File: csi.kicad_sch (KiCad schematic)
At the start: 90 parts, among them J701 WE_68715014522, J702 WE_68715014522, Q701 BSS138W-7-F, Q702 BSS138W-7-F, Q703 BSS138W-7-F, Q704 BSS138W-7-F, U701 PCA9547BS, U702 AP22615, U703 AP22615, U704 NX3DV642, U705 NX3DV642, U706 AP22615, U707 AP22615

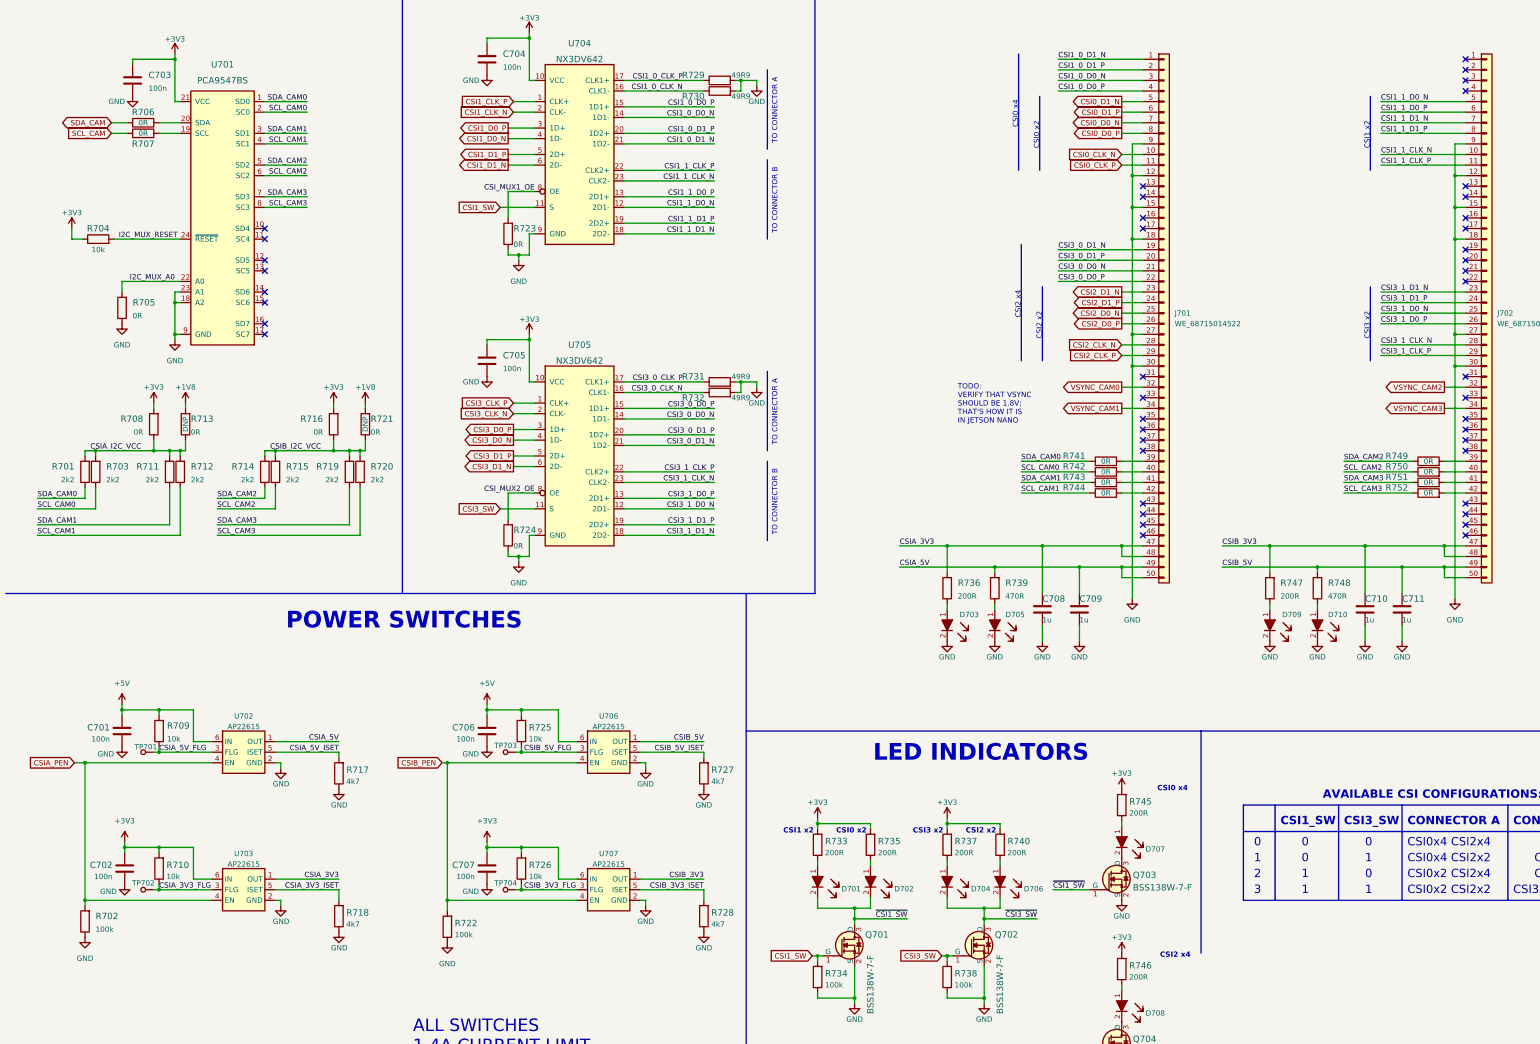
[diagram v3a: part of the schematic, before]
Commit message: Unified schematic look of ethernet sheet, improved shielding of eth connector, replaced gnd symbols
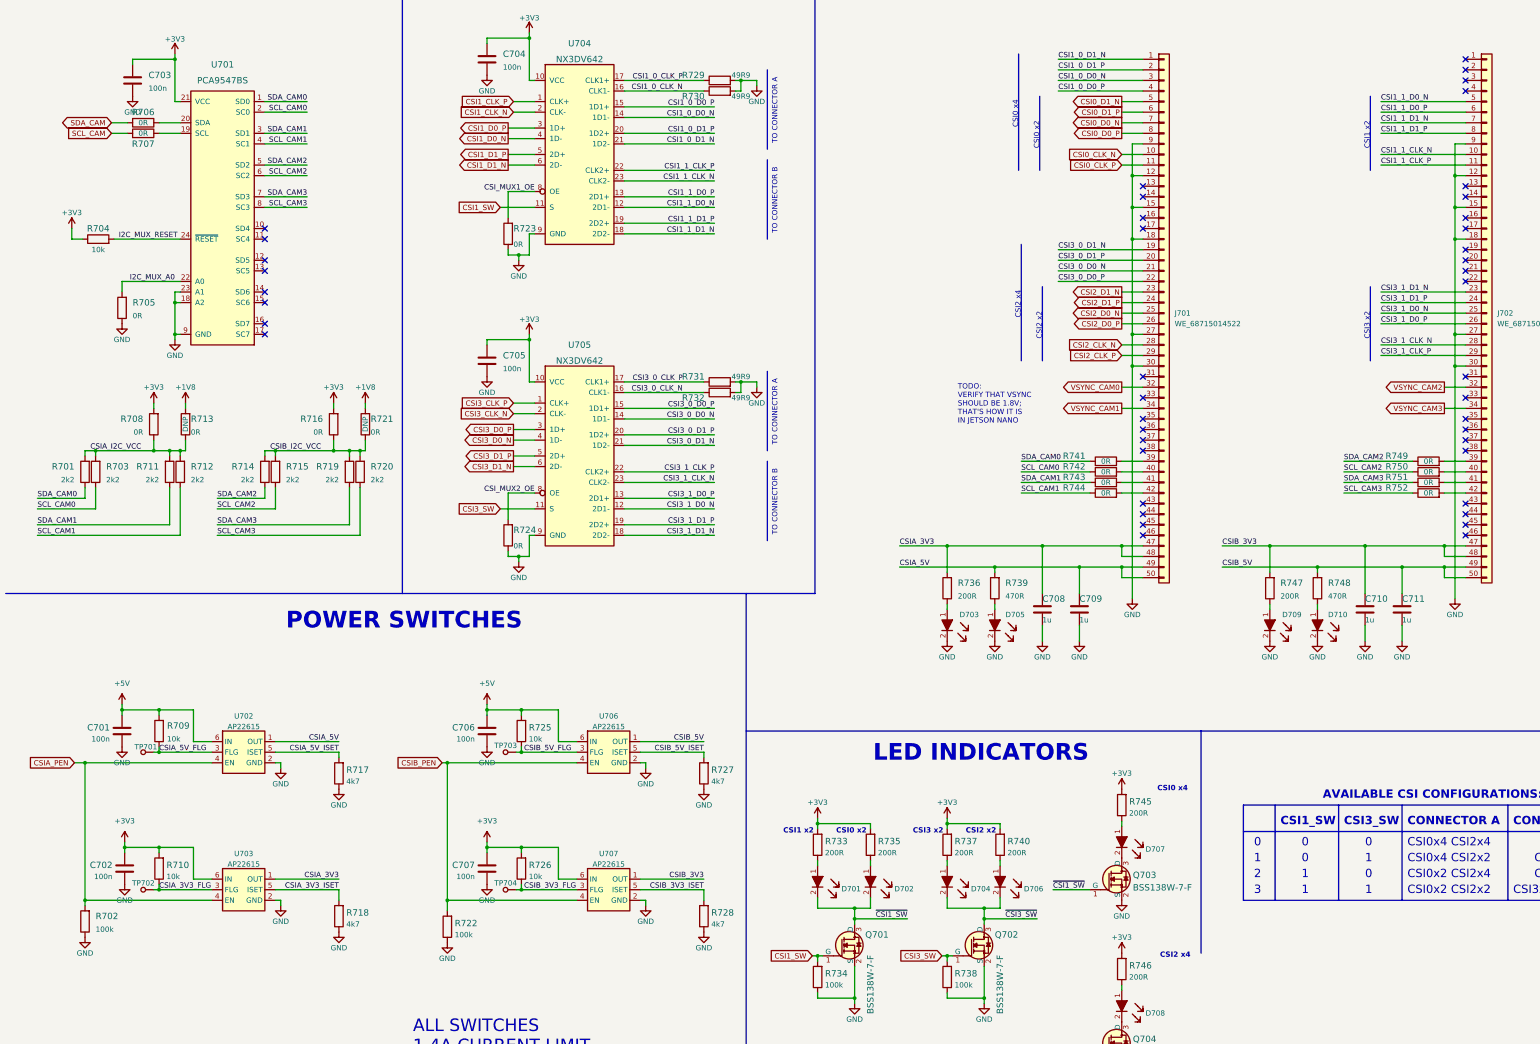
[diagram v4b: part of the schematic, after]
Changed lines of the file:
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@@
       (effects (font (size 1.27 1.27)) hide)
     )
-    (property "Value" "GND" (id 1) (at 135.89 91.44 0))
+    (property "Value" "GND" (id 1) (at 135.89 90.17 0))
     (property "Footprint" "" (id 2) (at 135.89 86.36 0)
       (effects (font (size 1.27 1.27)) hide)
@@
       (effects (font (size 1.27 1.27)) hide)
     )
-    (property "Value" "GND" (id 1) (at 283.21 172.72 0))
+    (property "Value" "GND" (id 1) (at 283.21 171.45 0))
     (property "Footprint" "" (id 2) (at 283.21 167.64 0)
       (effects (font (size 1.27 1.27)) hide)
@@
       (effects (font (size 1.27 1.27)) hide)
     )
-    (property "Value" "GND" (id 1) (at 118.745 255.27 0))
+    (property "Value" "GND" (id 1) (at 118.745 254 0))
     (property "Footprint" "" (id 2) (at 118.745 250.19 0)
       (effects (font (size 1.27 1.27)) hide)
@@
       (effects (font (size 1.27 1.27)) hide)
     )
-    (property "Value" "GND" (id 1) (at 31.75 254 0))
+    (property "Value" "GND" (id 1) (at 31.75 252.73 0))
     (property "Footprint" "" (id 2) (at 31.75 248.92 0)
       (effects (font (size 1.27 1.27)) hide)
@@
       (effects (font (size 1.27 1.27)) hide)
     )
-    (property "Value" "GND" (id 1) (at 90.805 251.46 0)
-      (effects (font (size 1.27 1.27)) (justify left))
-    )
+    (property "Value" "GND" (id 1) (at 92.71 251.46 0))
     (property "Footprint" "" (id 2) (at 92.71 247.65 0)
       (effects (font (size 1.27 1.27)) hide)
@@
       (effects (font (size 1.27 1.27)) hide)
     )
-    (property "Value" "GND" (id 1) (at 126.3651 237.9238 0)
-      (effects (font (size 1.27 1.27)) (justify left))
-    )
+    (property "Value" "GND" (id 1) (at 128.27 240.03 0))
     (property "Footprint" "" (id 2) (at 128.27 236.22 0)
       (effects (font (size 1.27 1.27)) hide)
@@
       (effects (font (size 1.27 1.27)) hide)
     )
-    (property "Value" "GND" (id 1) (at 126.3651 204.9038 0)
-      (effects (font (size 1.27 1.27)) (justify left))
-    )
+    (property "Value" "GND" (id 1) (at 128.27 207.01 0))
     (property "Footprint" "" (id 2) (at 128.27 203.2 0)
       (effects (font (size 1.27 1.27)) hide)
@@
       (effects (font (size 1.27 1.27)) hide)
     )
-    (property "Value" "GND" (id 1) (at 90.805 217.17 0)
-      (effects (font (size 1.27 1.27)) (justify left))
-    )
+    (property "Value" "GND" (id 1) (at 92.71 217.17 0))
     (property "Footprint" "" (id 2) (at 92.71 213.36 0)
       (effects (font (size 1.27 1.27)) hide)
@@
       (effects (font (size 1.27 1.27)) hide)
     )
-    (property "Value" "GND" (id 1) (at 76.835 245.11 0)
-      (effects (font (size 1.27 1.27)) (justify left))
-    )
+    (property "Value" "GND" (id 1) (at 78.74 245.11 0))
     (property "Footprint" "" (id 2) (at 78.74 241.3 0)
       (effects (font (size 1.27 1.27)) hide)
@@
       (effects (font (size 1.27 1.27)) hide)
     )
-    (property "Value" "GND" (id 1) (at 76.835 212.09 0)
-      (effects (font (size 1.27 1.27)) (justify left))
-    )
+    (property "Value" "GND" (id 1) (at 78.74 212.09 0))
     (property "Footprint" "" (id 2) (at 78.74 208.28 0)
       (effects (font (size 1.27 1.27)) hide)
@@
       (effects (font (size 1.27 1.27)) hide)
     )
-    (property "Value" "GND" (id 1) (at 39.3701 237.9238 0)
-      (effects (font (size 1.27 1.27)) (justify left))
-    )
+    (property "Value" "GND" (id 1) (at 41.275 240.03 0))
     (property "Footprint" "" (id 2) (at 41.275 236.22 0)
       (effects (font (size 1.27 1.27)) hide)
@@
       (effects (font (size 1.27 1.27)) hide)
     )
-    (property "Value" "GND" (id 1) (at 360.68 172.72 0))
+    (property "Value" "GND" (id 1) (at 360.68 171.45 0))
     (property "Footprint" "" (id 2) (at 360.68 167.64 0)
       (effects (font (size 1.27 1.27)) hide)
@@
       (effects (font (size 1.27 1.27)) hide)
     )
-    (property "Value" "GND" (id 1) (at 124.46 43.18 0))
+    (property "Value" "GND" (id 1) (at 128.27 45.72 0))
     (property "Footprint" "" (id 2) (at 128.27 41.91 0)
       (effects (font (size 1.27 1.27)) hide)
@@
       (effects (font (size 1.27 1.27)) hide)
     )
-    (property "Value" "GND" (id 1) (at 135.89 163.83 0))
+    (property "Value" "GND" (id 1) (at 135.89 162.56 0))
     (property "Footprint" "" (id 2) (at 135.89 158.75 0)
       (effects (font (size 1.27 1.27)) hide)
@@
       (effects (font (size 1.27 1.27)) hide)
     )
-    (property "Value" "GND" (id 1) (at 39.37 48.26 0))
+    (property "Value" "GND" (id 1) (at 43.18 50.8 0))
     (property "Footprint" "" (id 2) (at 43.18 46.99 0)
       (effects (font (size 1.27 1.27)) hide)
@@
       (effects (font (size 1.27 1.27)) hide)
     )
-    (property "Value" "GND" (id 1) (at 40.64 106.68 0))
+    (property "Value" "GND" (id 1) (at 40.64 105.41 0))
     (property "Footprint" "" (id 2) (at 40.64 101.6 0)
       (effects (font (size 1.27 1.27)) hide)
@@
       (effects (font (size 1.27 1.27)) hide)
     )
-    (property "Value" "GND" (id 1) (at 124.46 115.57 0))
+    (property "Value" "GND" (id 1) (at 128.27 118.11 0))
     (property "Footprint" "" (id 2) (at 128.27 114.3 0)
       (effects (font (size 1.27 1.27)) hide)
@@
       (effects (font (size 1.27 1.27)) hide)
     )
-    (property "Value" "GND" (id 1) (at 38.7351 204.9038 0)
-      (effects (font (size 1.27 1.27)) (justify left))
-    )
+    (property "Value" "GND" (id 1) (at 40.64 207.01 0))
     (property "Footprint" "" (id 2) (at 40.64 203.2 0)
       (effects (font (size 1.27 1.27)) hide)
@@
       (effects (font (size 1.27 1.27)) hide)
     )
-    (property "Value" "GND" (id 1) (at 53.34 110.49 0))
+    (property "Value" "GND" (id 1) (at 53.34 109.22 0))
     (property "Footprint" "" (id 2) (at 53.34 105.41 0)
       (effects (font (size 1.27 1.27)) hide)

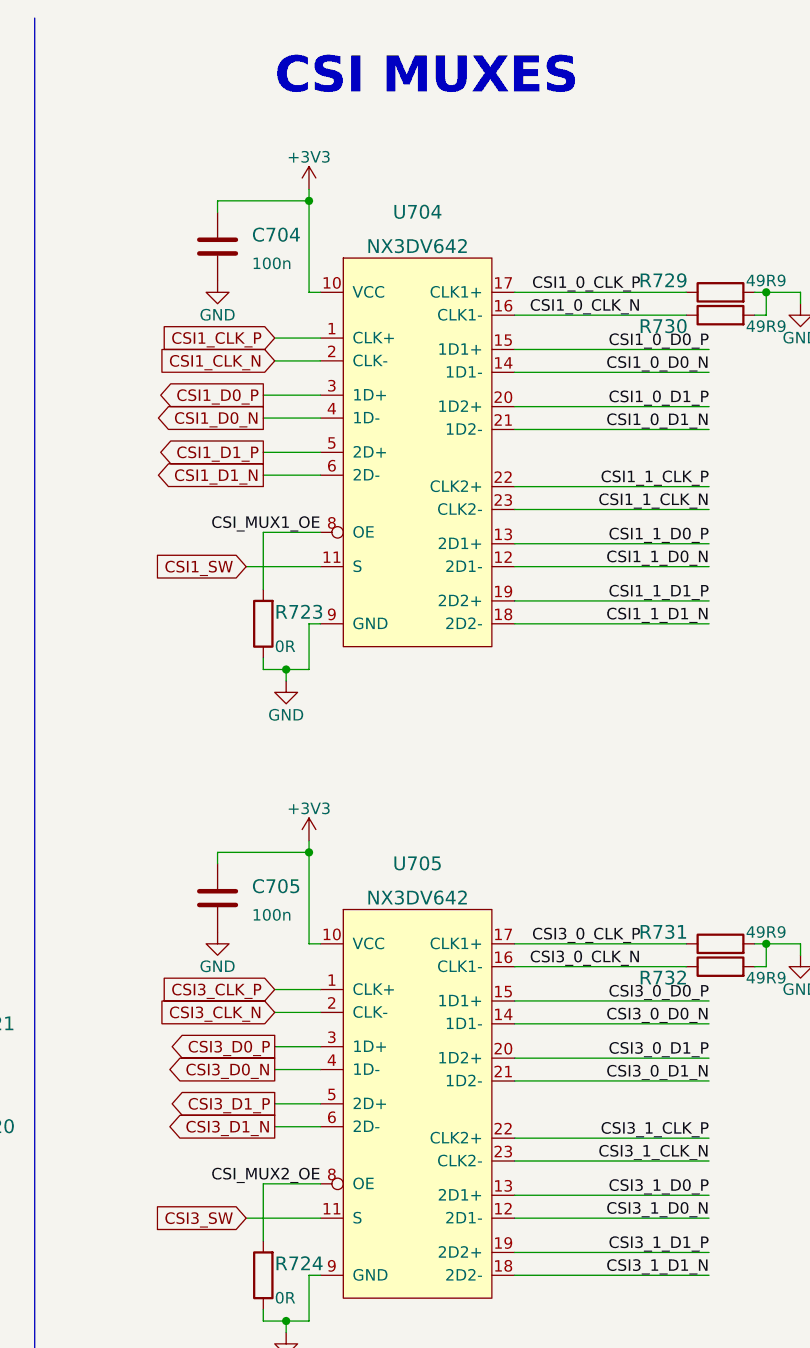
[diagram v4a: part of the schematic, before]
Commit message: Add CSI MUX labels and numbers to refer to on Block Diagram, update all GND symbols from global library
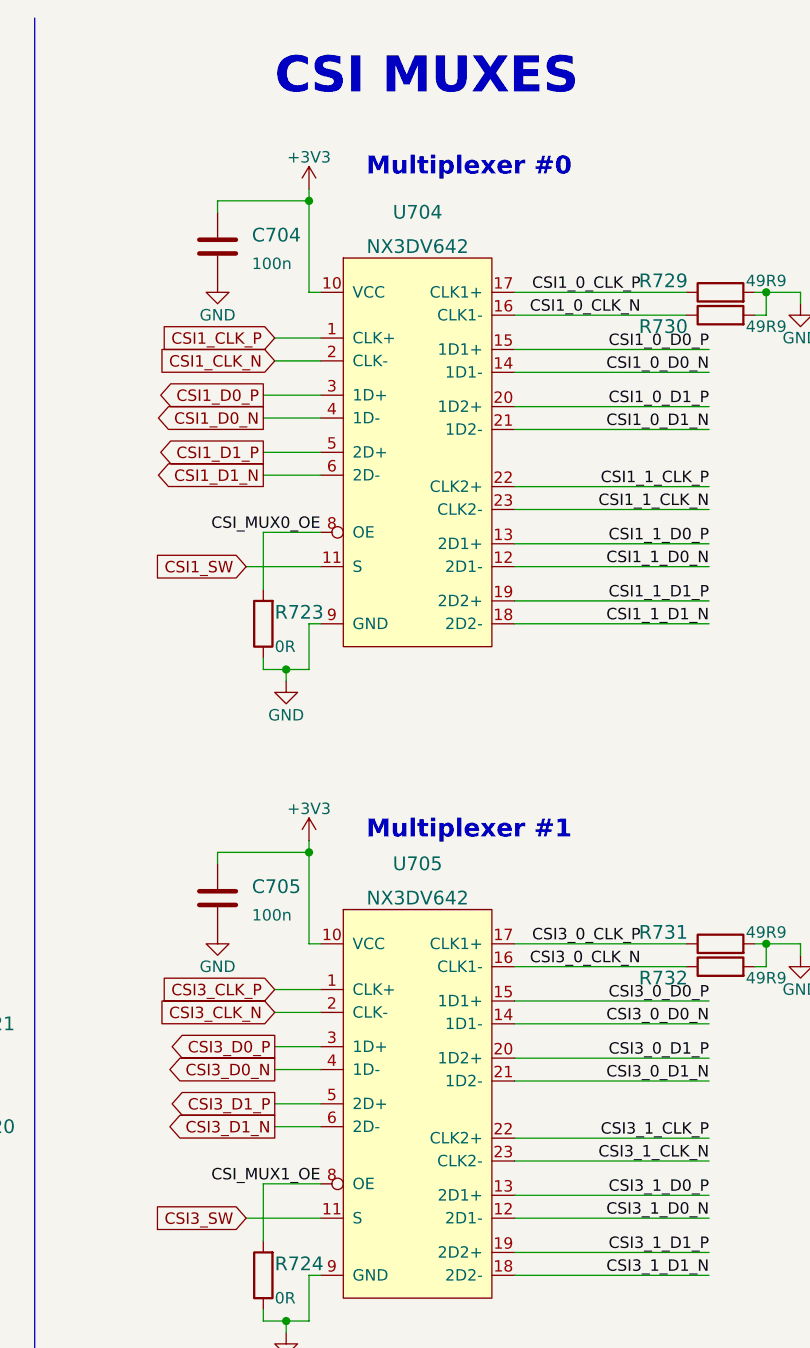
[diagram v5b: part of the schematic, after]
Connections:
- net CSI_MUX2_OE is gone; now on net CSI_MUX1_OE: R724.2, U705.8 (OE)
- net CSI_MUX1_OE: no longer R723.2, U704.8 (OE)
- new net CSI_MUX0_OE: R723.2, U704.8 (OE)
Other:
- note added: "Multiplexer #0"
- note added: "Multiplexer #1"

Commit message: SCH: Update title block, set revision to 1.0.0
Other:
- title: Jetson Orin NX Baseboard -> Jetson Orin Baseboard
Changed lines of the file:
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@@
   (paper "A3")
   (title_block
-    (title "Jetson Orin NX Baseboard")
+    (title "Jetson Orin Baseboard")
     (date "2022-09-28")
-    (rev "0.1.0")
+    (rev "1.0.0")
     (company "Antmicro Ltd")
     (comment 1 "www.antmicro.com")
